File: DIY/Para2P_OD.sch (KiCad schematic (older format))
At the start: 6 parts, among them J1 Atari_SEGA_DE9, J2 Atari_SEGA_DE9, J3 DB25_Male, U1 74AHCT125N, U2 74AHCT125N, U3 74AHCT125N

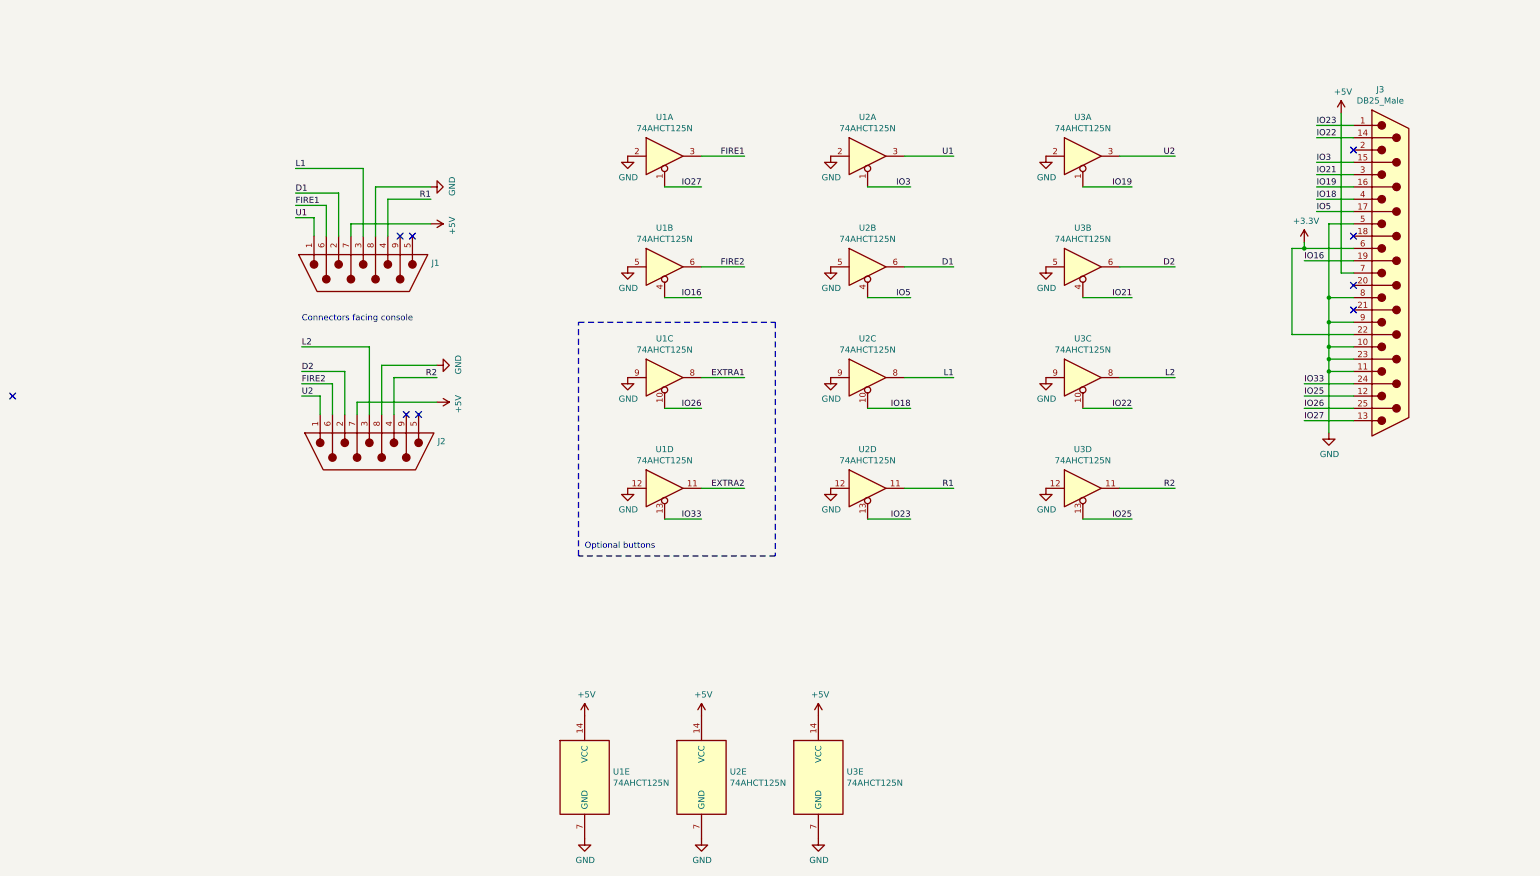
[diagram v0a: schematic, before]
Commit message: Simplify parallel schematics
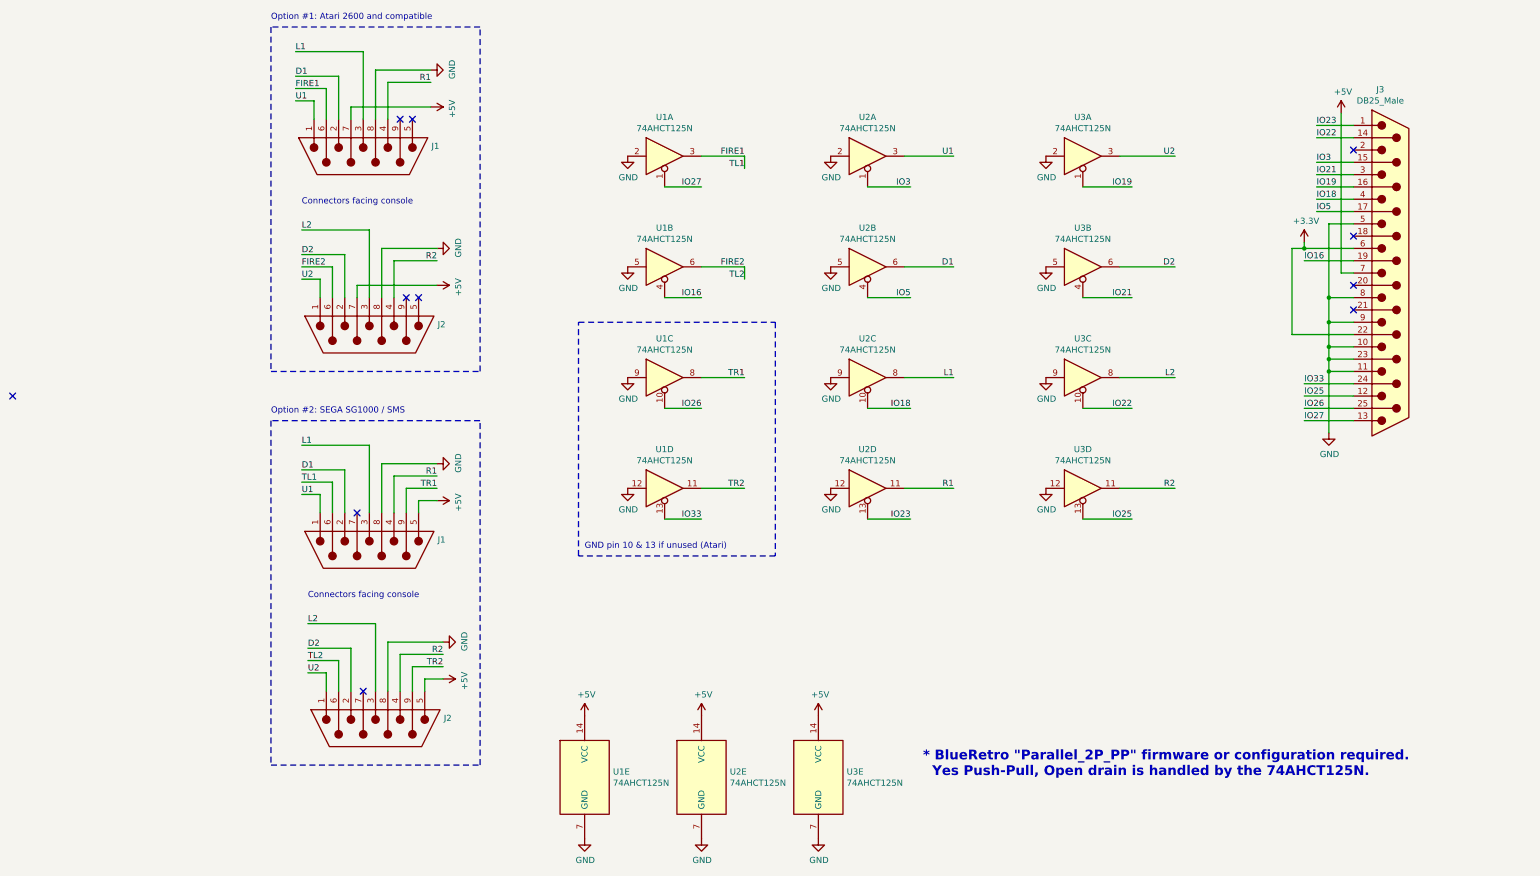
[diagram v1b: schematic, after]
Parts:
- added J1, J2: Atari_SEGA_DE9, symbol Connector_Gaming:Atari_SEGA_DE9
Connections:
- net +5V: now also J1.5, J2.5
- net D1: now also J1.2
- net D2: now also J2.2
- net FIRE1: now also J1.6
- net FIRE2: now also J2.6
- net GND: now also J1.8, J2.8
- net L1: now also J1.3
- net L2: now also J2.3
- net R1: now also J1.4
- net R2: now also J2.4
- net U1: now also J1.1
- net U2: now also J2.1
- net EXTRA1 renamed TR1
- net TR1: now also J1.9
- net EXTRA2 renamed TR2
- net TR2: now also J2.9
- no-connect marks 9 -> 11
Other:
- note added: "* BlueRetro "Parallel_2P_PP" firmware or configuration required.\n Yes Push-Pull, Open drain is handled by the 74AHCT125N."
- note added: "GND pin 10 & 13 if unused (Atari)"
- note added: "Option #1: Atari 2600 and compatible"
- note added: "Option #2: SEGA SG1000 / SMS"
- note removed: "Optional buttons"
- moved on the sheet: J1, J2
